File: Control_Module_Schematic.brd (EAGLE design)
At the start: 67 x 47 mm, 28 parts, among them U2 ATMEGA328P_TQFP

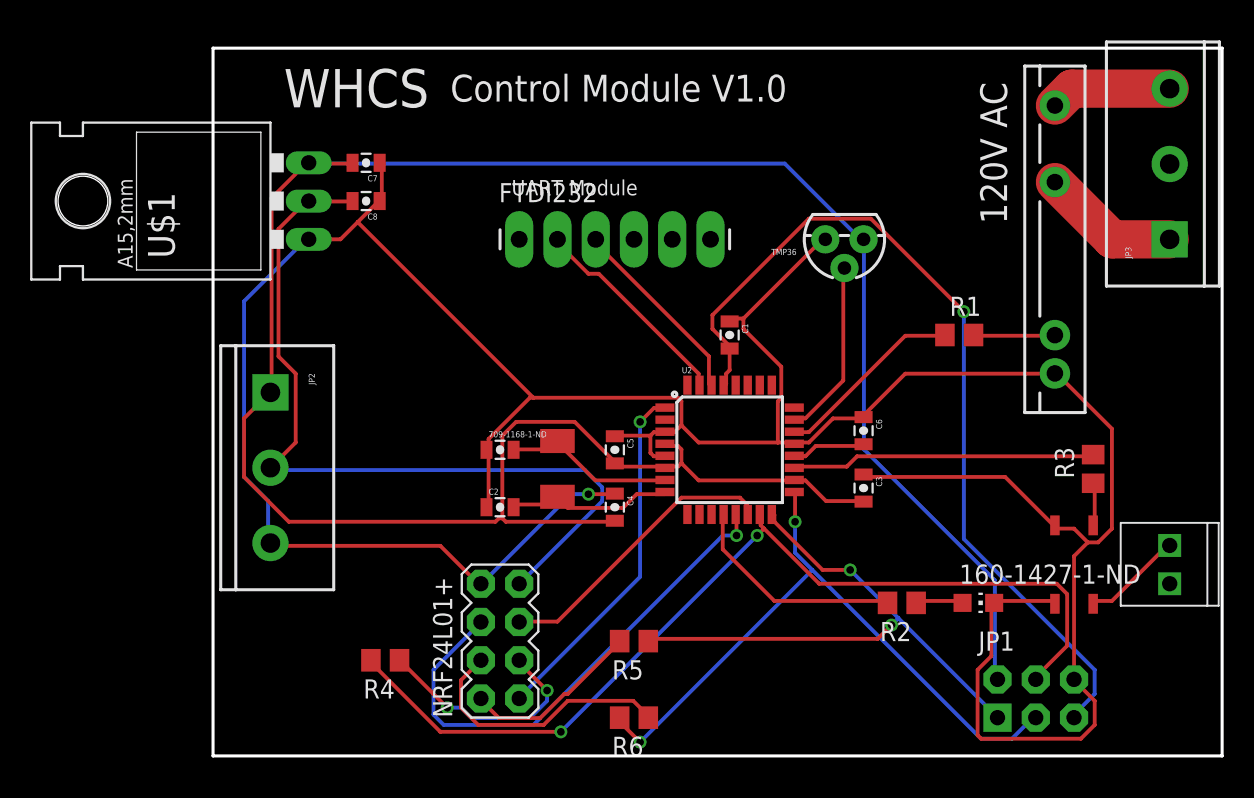
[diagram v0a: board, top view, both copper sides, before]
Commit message: Board status when first submitted.
This is the way the board was when first submitted to Oshpark for an
initial run.
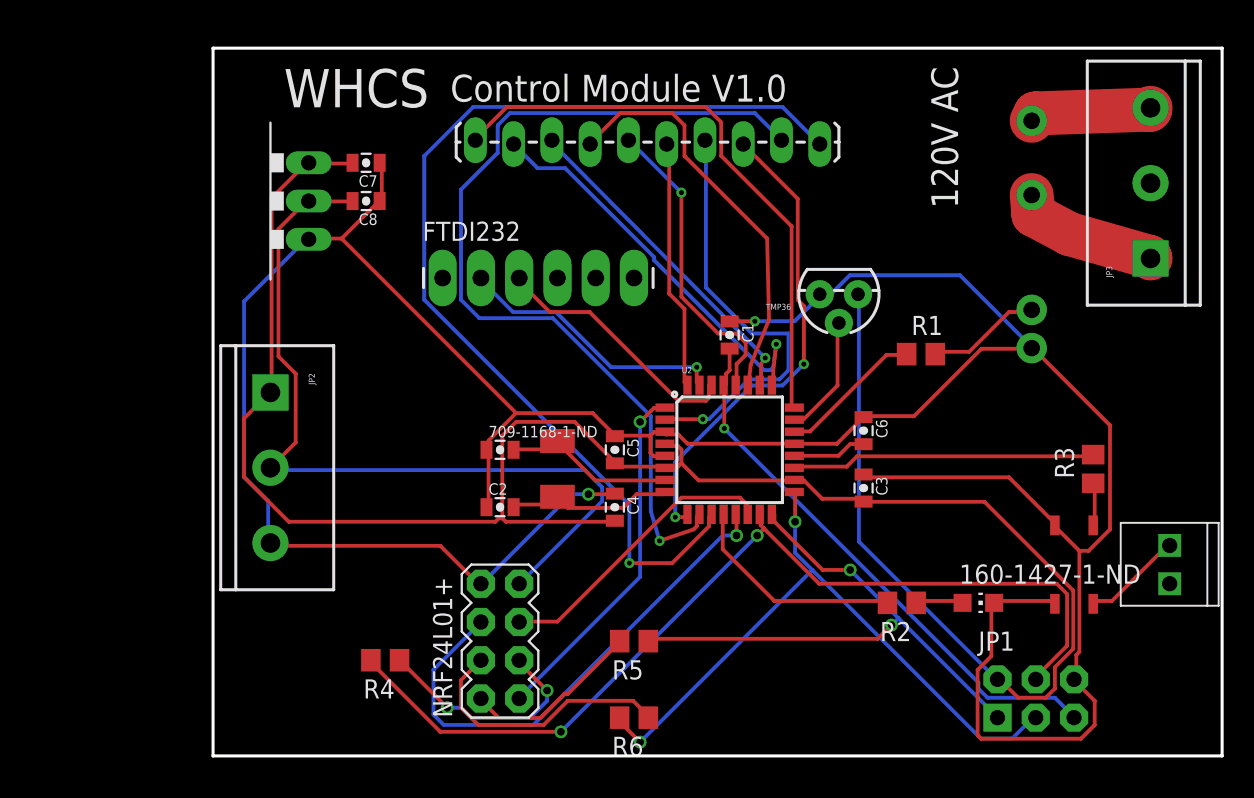
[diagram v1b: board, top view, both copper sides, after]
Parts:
- added JP4: (no value), SparkFun-Connectors:1X10_LOCK_LONGPADS
- JP1: value AVR_SPI_PRG_6NS -> AVR_SPI
- SSR: device SparkFun-Electromechanical:RELAY-S108T02 -> WHCS:RELAY-S116S02F
- U$1: value V_REG_LD1117VXX -> LD1117VXX
- moved FTDI232 5.69 mm to (15.2, 31.7)
- moved TMP36 3.66 mm to (41.5, 30.6)
- moved R1 2.84 mm to (47.0, 26.7)
- moved SSR 2.62 mm to (53.3, 34.7)
- moved JP3 1.80 mm to (62.2, 33.0)
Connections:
- new net PC1: JP4.1, U2.24
- new net PC2: JP4.2, U2.25
- new net PC3: JP4.3, U2.26
- new net PC4: JP4.4, U2.27
- new net PC5: JP4.5, U2.28
- new net PD2: JP4.6, U2.32
- new net PD4: JP4.7, U2.2
- new net PD5: JP4.8, U2.9
- new net PD6: JP4.9, U2.10
- new net PD7: JP4.10, U2.11
- net 3.3V: now also U$1.OUT; no longer U$1.GND
- net 5V: now also U$1.IN; no longer U$1.OUT
- net GND: now also SSR.P$4, U$1.GND; no longer SSR.4, U$1.IN
- net N$10: now also SSR.P$1; no longer SSR.1
- net N$11: now also SSR.P$2; no longer SSR.2
- net N$8: now also SSR.P$3; no longer SSR.3
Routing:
- net PD7: track 0.00 -> 68.4 mm, vias 0 -> 1
- net PD6: track 0.00 -> 60.2 mm, vias 0 -> 1
- net PC1: track 0.00 -> 38.7 mm
- net PD5: track 0.00 -> 32.0 mm, vias 0 -> 2
- net PD4: track 0.00 -> 28.6 mm, vias 0 -> 1
- net PC2: track 0.00 -> 28.0 mm, vias 0 -> 1
- net PC4: track 0.00 -> 27.3 mm
- net PC3: track 0.00 -> 22.4 mm, vias 0 -> 1
- net N$24: track 58.3 -> 37.0 mm
- net PC5: track 0.00 -> 20.5 mm, vias 0 -> 1
- net PD2: track 0.00 -> 16.6 mm
- net 5V: track 158.2 -> 143.7 mm
- net TXD: track 14.0 -> 18.2 mm, vias 0 -> 1
- net RXD: track 13.0 -> 17.2 mm
- net N$7: track 11.8 -> 8.00 mm
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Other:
- board text added: "Test points. solid state relay considerations."
- board text removed: "UART Module"

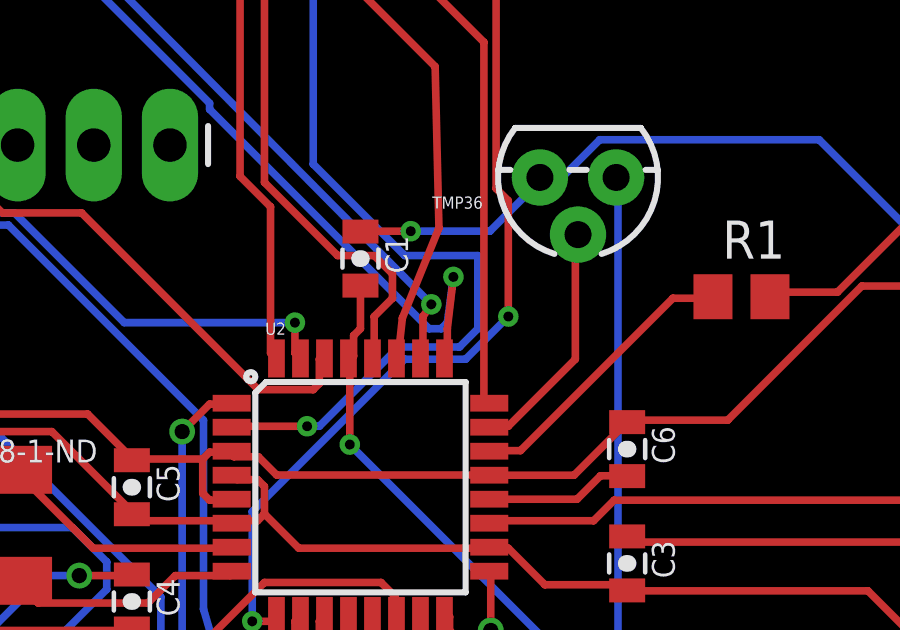
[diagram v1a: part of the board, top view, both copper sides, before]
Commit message: fixed drc fail. Two vias were too close together at the top right of the mcu
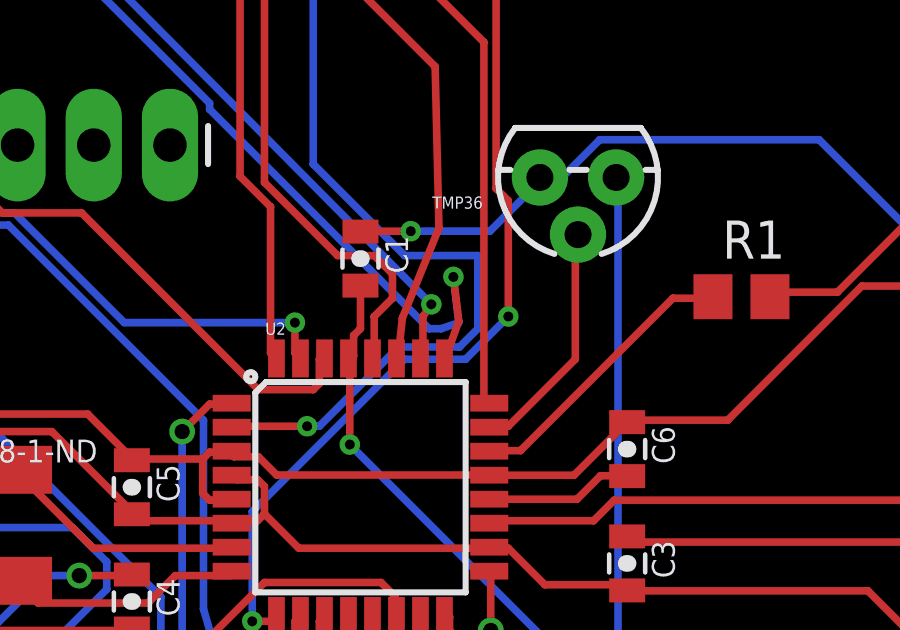
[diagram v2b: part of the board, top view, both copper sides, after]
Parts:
- added FRAME1: FRAME-LETTERNO_PACKAGE, WHCS:DUMMY
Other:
- board text removed: "Test points. solid state relay considerations."
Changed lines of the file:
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@@
 <text x="15.748" y="43.434" size="1.778" layer="21">Control Module V1.0</text>
 <text x="49.4538" y="36.3347" size="1.778" layer="21" rot="R90">120V AC</text>
-<text x="6.35" y="52.07" size="1.778" layer="51">Test points.
-solid state relay considerations.</text>
 </plain>
 <attributes>
@@
 <attribute name="VALUE" x="16.1417" y="37.5666" size="1.27" layer="27" font="vector"/>
 </element>
+<element name="FRAME1" library="WHCS" package="DUMMY" value="FRAME-LETTERNO_PACKAGE" x="0" y="-1.27">
+<attribute name="VERSION" value="v01" x="0" y="-1.27" size="1.778" layer="27" display="off"/>
+<attribute name="DESIGNER" value="Nobody" x="0" y="-1.27" size="1.778" layer="27" display="off"/>
+</element>
 </elements>
 <signals>
@@
 <contactref element="JP4" pad="2"/>
 <contactref element="U2" pad="25"/>
-<wire x1="37.1856" y1="25.6032" x2="37.1856" y2="24.7904" width="0.254" layer="1"/>
-<wire x1="37.3888" y1="27.3304" x2="37.1856" y2="25.6032" width="0.254" layer="1"/>
-<wire x1="37.1856" y1="25.8064" x2="37.3888" y2="27.3304" width="0.254" layer="16"/>
-<wire x1="36.9824" y1="25.6032" x2="37.1856" y2="25.8064" width="0.254" layer="16"/>
+<wire x1="37.5666" y1="25.8572" x2="37.1856" y2="24.7904" width="0.254" layer="1"/>
+<wire x1="37.3888" y1="27.3304" x2="37.5666" y2="25.8572" width="0.254" layer="1"/>
+<wire x1="37.5666" y1="25.8064" x2="37.3888" y2="27.3304" width="0.254" layer="16"/>
+<wire x1="36.9824" y1="25.6032" x2="37.5666" y2="25.8064" width="0.254" layer="16"/>
 <wire x1="36.576" y1="25.6032" x2="36.9824" y2="25.6032" width="0.254" layer="16"/>
 <wire x1="29.2608" y1="32.9184" x2="36.576" y2="25.6032" width="0.254" layer="16"/>
@@
 </board>
 </drawing>
-<compatibility>
-<note version="6.3" minversion="6.2.2" severity="warning">
-Since Version 6.2.2 text objects can contain more than one line,
-which will not be processed correctly with this version.
-</note>
-</compatibility>
 </eagle>

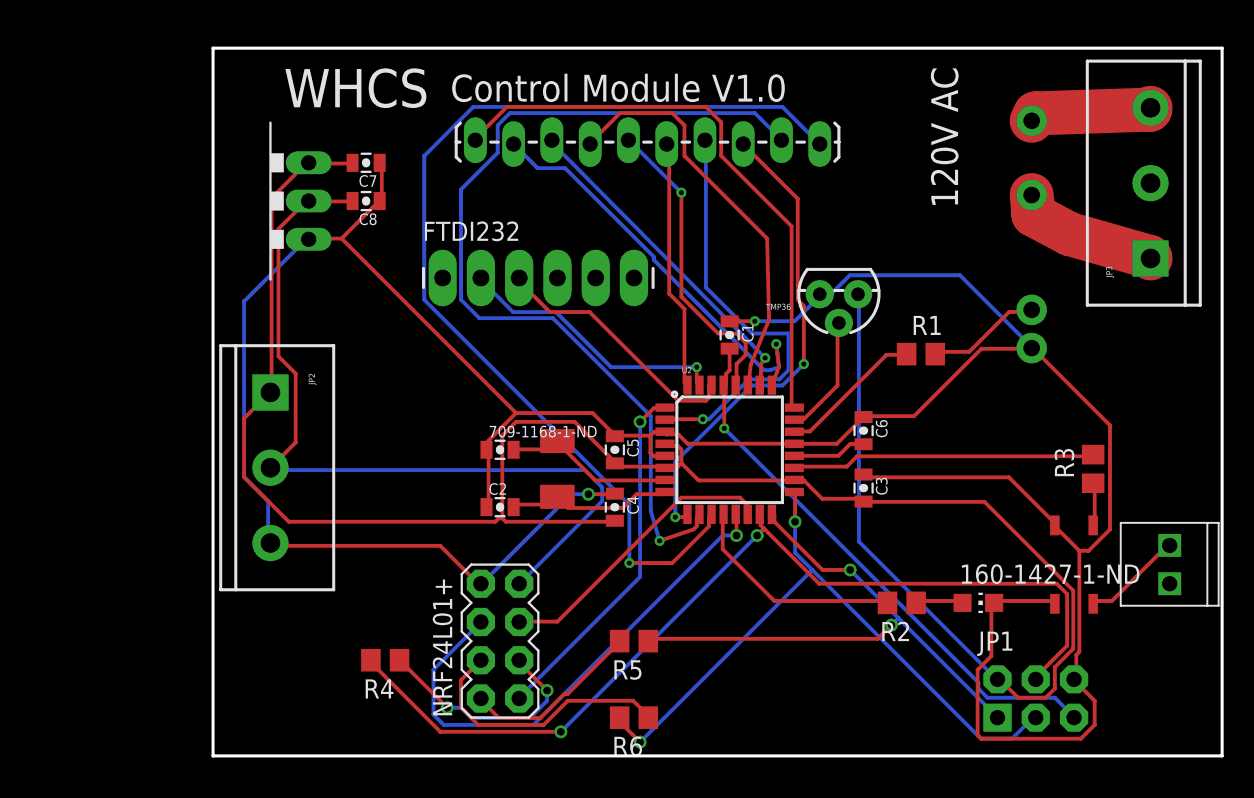
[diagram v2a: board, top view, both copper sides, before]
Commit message: Changed the pin that controls the door strike
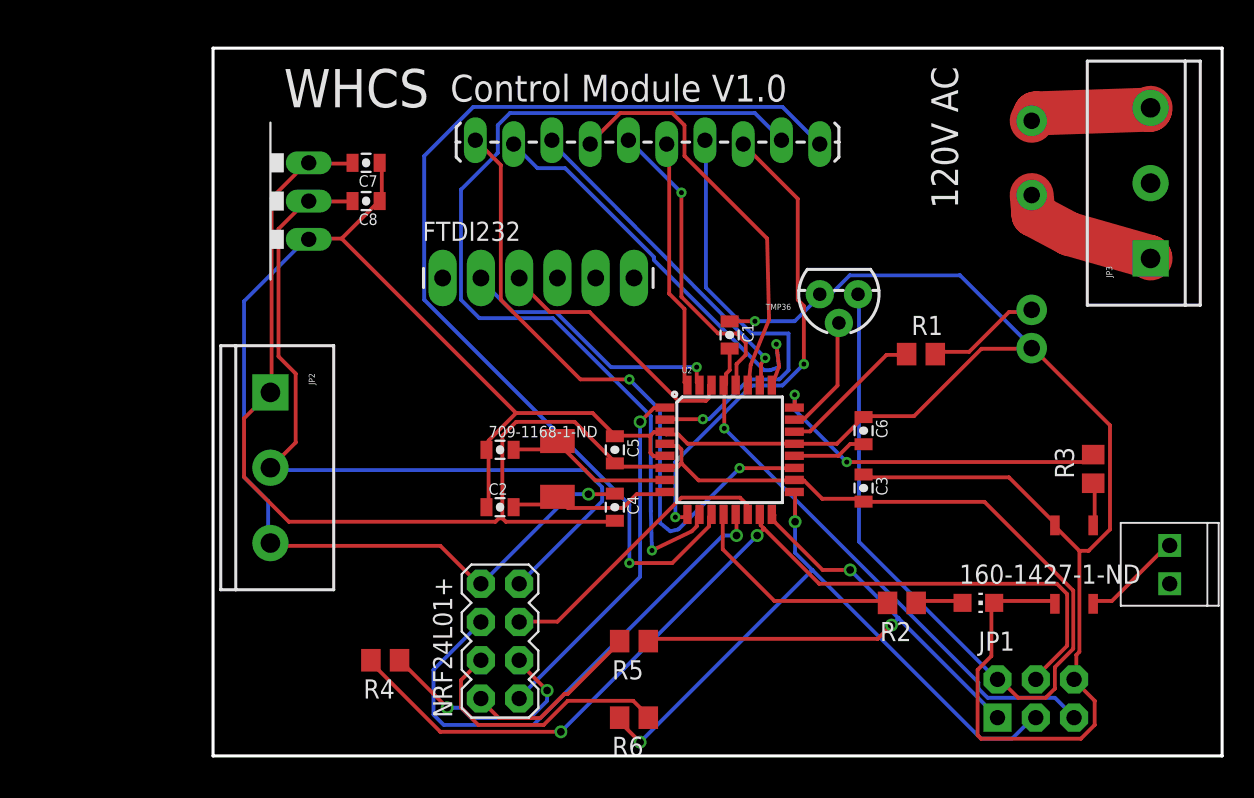
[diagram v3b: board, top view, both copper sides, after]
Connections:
- removed net N$19: R3.2, U2.19
- removed net PC1: JP4.1, U2.24
- new net ADC6: JP4.1, U2.19
- new net N$12: R3.2, U2.24
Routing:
- net ADC6: track 0.00 -> 43.2 mm, vias 0 -> 2
- net PC1: track 38.7 -> 0.00 mm
- net N$12: track 0.00 -> 23.3 mm, vias 0 -> 2
- net N$19: track 20.2 -> 0.00 mm
- net PD6: track 60.2 -> 61.5 mm
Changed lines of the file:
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@@
 <wire x1="46.863" y1="10.287" x2="46.67" y2="10.16" width="0.254" layer="1"/>
-</signal>
-<signal name="N$19">
-<contactref element="R3" pad="2"/>
-<contactref element="U2" pad="19"/>
-<wire x1="42.0624" y1="19.2024" x2="38.6334" y2="19.2024" width="0.254" layer="1"/>
-<wire x1="42.7482" y1="19.8882" x2="42.0624" y2="19.2024" width="0.254" layer="1"/>
-<wire x1="58.293" y1="19.8882" x2="42.7482" y2="19.8882" width="0.254" layer="1"/>
-<wire x1="38.6334" y1="19.2024" x2="38.5826" y2="19.12" width="0.254" layer="1"/>
-<wire x1="58.293" y1="19.8882" x2="58.42" y2="20" width="0.254" layer="1"/>
 </signal>
 <signal name="N$13">
@@
 <wire x1="62.1792" y1="42.8752" x2="62.23" y2="43.02" width="2.921" layer="1"/>
 </signal>
-<signal name="PC1">
-<contactref element="JP4" pad="1"/>
-<contactref element="U2" pad="24"/>
-<wire x1="38.4048" y1="35.1536" x2="38.4048" y2="23.1648" width="0.254" layer="1"/>
-<wire x1="33.7312" y1="39.8272" x2="38.4048" y2="35.1536" width="0.254" layer="1"/>
-<wire x1="33.7312" y1="42.0624" x2="33.7312" y2="39.8272" width="0.254" layer="1"/>
-<wire x1="32.7152" y1="43.0784" x2="33.7312" y2="42.0624" width="0.254" layer="1"/>
-<wire x1="19.5072" y1="43.0784" x2="32.7152" y2="43.0784" width="0.254" layer="1"/>
-<wire x1="17.4752" y1="41.0464" x2="19.5072" y2="43.0784" width="0.254" layer="1"/>
-<wire x1="38.4048" y1="23.1648" x2="38.5826" y2="23.12" width="0.254" layer="1"/>
-<wire x1="17.4752" y1="41.0464" x2="17.4117" y2="40.8686" width="0.254" layer="1"/>
-</signal>
 <signal name="PC2">
 <contactref element="JP4" pad="2"/>
@@
 <contactref element="U2" pad="10"/>
 <wire x1="32.1056" y1="15.24" x2="32.1056" y2="15.8496" width="0.254" layer="1"/>
-<wire x1="31.9024" y1="15.0368" x2="32.1056" y2="15.24" width="0.254" layer="1"/>
-<wire x1="29.6418" y1="14.2748" x2="31.9024" y2="15.0368" width="0.254" layer="1"/>
-<wire x1="29.0576" y1="16.256" x2="29.6418" y2="14.2748" width="0.254" layer="16"/>
+<wire x1="31.7754" y1="14.9098" x2="32.1056" y2="15.24" width="0.254" layer="1"/>
+<wire x1="29.1338" y1="13.6398" x2="31.7754" y2="14.9098" width="0.254" layer="1"/>
+<wire x1="29.0576" y1="16.256" x2="29.1338" y2="13.6398" width="0.254" layer="16"/>
 <wire x1="29.0576" y1="22.5552" x2="29.0576" y2="16.256" width="0.254" layer="16"/>
 <wire x1="22.5552" y1="29.0576" x2="29.0576" y2="22.5552" width="0.254" layer="16"/>
@@
 <wire x1="32.1056" y1="15.8496" x2="32.29" y2="16.0274" width="0.254" layer="1"/>
 <wire x1="37.592" y1="41.0464" x2="37.7317" y2="40.8686" width="0.254" layer="16"/>
-<via x="29.6418" y="14.2748" extent="1-16" drill="0.3302"/>
+<via x="29.1338" y="13.6398" extent="1-16" drill="0.3302"/>
 </signal>
 <signal name="PD7">
@@
 <via x="27.6352" y="12.8016" extent="1-16" drill="0.3302"/>
 </signal>
+<signal name="N$12">
+<contactref element="U2" pad="24"/>
+<contactref element="R3" pad="2"/>
+<wire x1="38.608" y1="23.9776" x2="38.608" y2="23.1648" width="0.254" layer="1"/>
+<wire x1="38.608" y1="22.9616" x2="38.608" y2="23.9776" width="0.254" layer="16"/>
+<wire x1="42.0624" y1="19.5072" x2="38.608" y2="22.9616" width="0.254" layer="16"/>
+<wire x1="57.912" y1="19.5072" x2="42.0624" y2="19.5072" width="0.254" layer="1"/>
+<wire x1="58.3184" y1="19.9136" x2="57.912" y2="19.5072" width="0.254" layer="1"/>
+<wire x1="38.608" y1="23.1648" x2="38.5826" y2="23.12" width="0.254" layer="1"/>
+<wire x1="58.3184" y1="19.9136" x2="58.42" y2="20" width="0.254" layer="1"/>
+<via x="38.608" y="23.9776" extent="1-16" drill="0.3302"/>
+<via x="42.0624" y="19.5072" extent="1-16" drill="0.3302"/>
+</signal>
+<signal name="ADC6">
+<contactref element="JP4" pad="1"/>
+<contactref element="U2" pad="19"/>
+<wire x1="34.9504" y1="19.1008" x2="38.4048" y2="19.1008" width="0.254" layer="1"/>
+<wire x1="30.8864" y1="15.0368" x2="34.9504" y2="19.1008" width="0.254" layer="16"/>
+<wire x1="30.353" y1="14.9098" x2="30.8864" y2="15.0368" width="0.254" layer="16"/>
+<wire x1="29.6672" y1="15.4686" x2="30.353" y2="14.9098" width="0.254" layer="16"/>
+<wire x1="29.6672" y1="22.9616" x2="29.6672" y2="15.4686" width="0.254" layer="16"/>
+<wire x1="27.6352" y1="24.9936" x2="29.6672" y2="22.9616" width="0.254" layer="16"/>
+<wire x1="24.384" y1="24.9936" x2="27.6352" y2="24.9936" width="0.254" layer="1"/>
+<wire x1="19.1008" y1="30.2768" x2="24.384" y2="24.9936" width="0.254" layer="1"/>
+<wire x1="19.1008" y1="39.2176" x2="19.1008" y2="30.2768" width="0.254" layer="1"/>
+<wire x1="17.4752" y1="40.8432" x2="19.1008" y2="39.2176" width="0.254" layer="1"/>
+<wire x1="38.4048" y1="19.1008" x2="38.5826" y2="19.12" width="0.254" layer="1"/>
+<wire x1="17.4752" y1="40.8432" x2="17.4117" y2="40.8686" width="0.254" layer="1"/>
+<via x="34.9504" y="19.1008" extent="1-16" drill="0.3302"/>
+<via x="27.6352" y="24.9936" extent="1-16" drill="0.3302"/>
+</signal>
 </signals>
